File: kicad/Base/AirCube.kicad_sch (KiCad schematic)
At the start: 44 parts, among them P1 USB_C_Plug_USB2.0, Q1 BSS138, U10 ENS210, U2 ENS161, U5 AP2120, U6 AP2205, U7 ESP32-H2-MINI-1

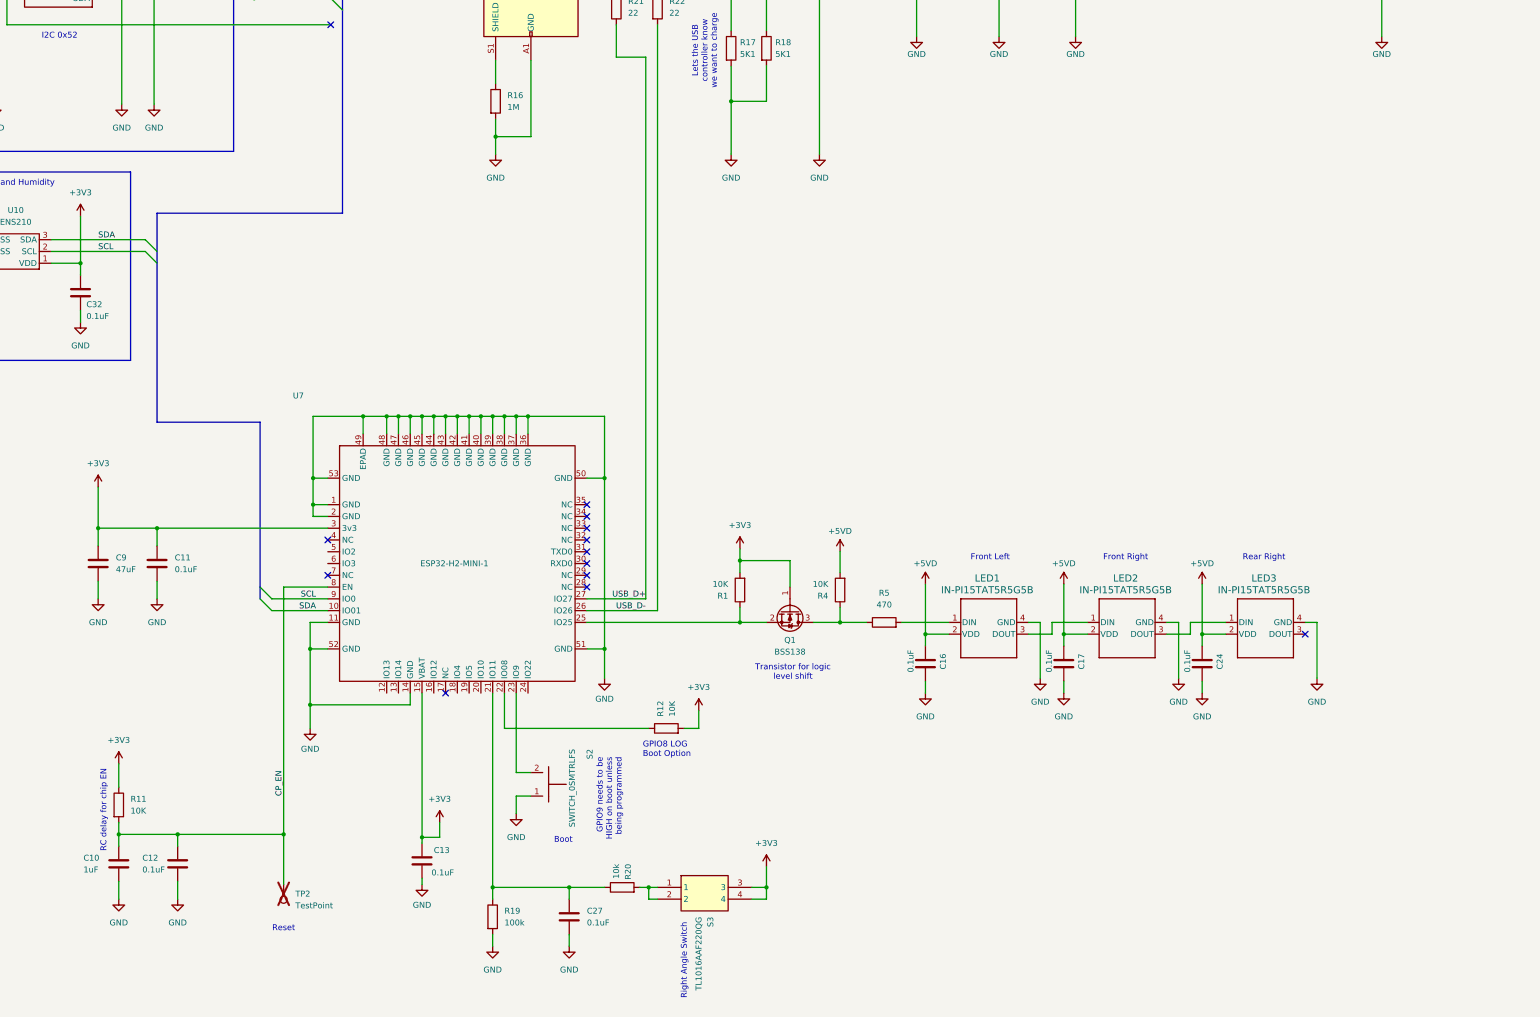
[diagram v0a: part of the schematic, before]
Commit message: Replace H2 schematic with S3 and add PM UART and modem control nets
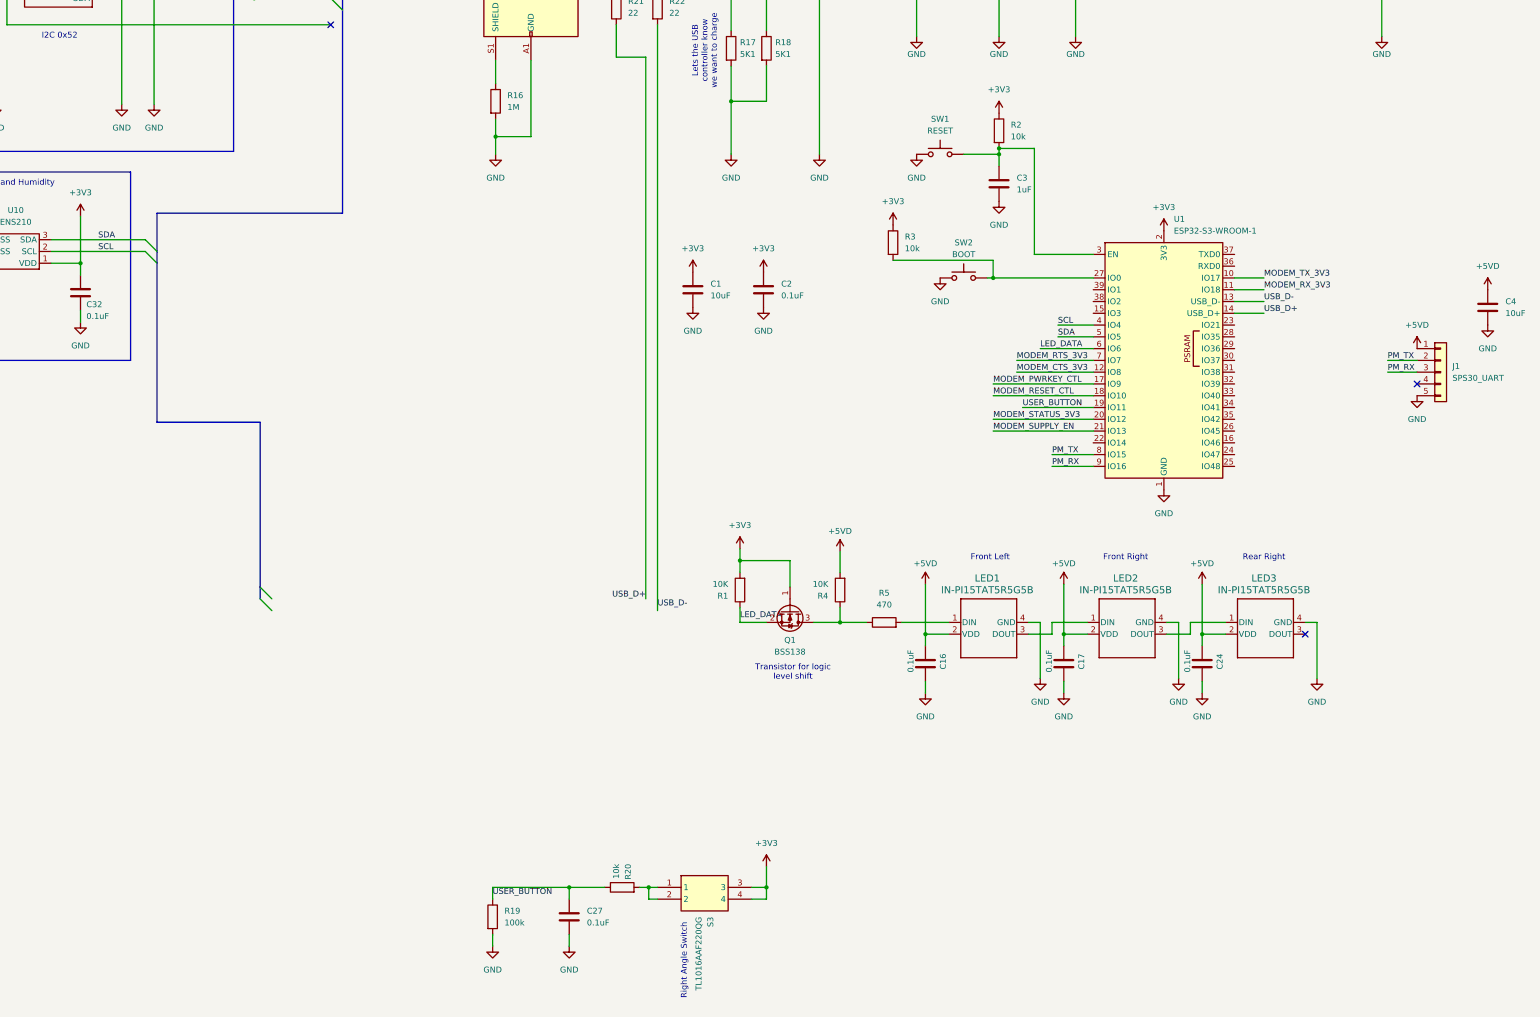
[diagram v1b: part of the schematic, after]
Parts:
- removed C10: 1uF, Capacitor_SMD:C_0603_1608Metric, symbol Device:C
- removed C11, C12, C13: 0.1uF, Capacitor_SMD:C_0603_1608Metric, symbol Device:C
- removed C9: 47uF, Capacitor_SMD:C_0603_1608Metric, symbol Device:C
- removed R11, R12: 10K, Resistor_SMD:R_0603_1608Metric, symbol Device:R
- removed S2: SWITCH_0SMTRLFS, kicad_reformed_custom_IC:SWITCH_0SMTRLFS, symbol custom_IC:TL4100AF240QG_
- removed TP2: TestPoint, TestPoint:TestPoint_Pad_1.5x1.5mm, symbol Connector:TestPoint
- removed U7: ESP32-H2-MINI-1, kicad_reformed_custom_IC:MODULE_ESP32-H2-MINI-1-H2, symbol custom_IC:ESP32-H2-MINI-1
- added C1, C4: 10uF, Capacitor_SMD:C_0805_2012Metric, symbol Device:C
- added C2: 0.1uF, Capacitor_SMD:C_0603_1608Metric, symbol Device:C
- added C3: 1uF, Capacitor_SMD:C_0603_1608Metric, symbol Device:C
- added J1: SPS30_UART, symbol Connector_Generic:Conn_01x05
- added R2, R3: 10k, Resistor_SMD:R_0603_1608Metric, symbol Device:R
- added SW1: RESET, symbol Switch:SW_Push
- added SW2: BOOT, symbol Switch:SW_Push
- added U1: ESP32-S3-WROOM-1, RF_Module:ESP32-S3-WROOM-1, symbol RF_Module:ESP32-S3-WROOM-1
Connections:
- net +3V3: now also C1.1, C2.1, R2.1, R3.1, U1.2 (3V3)
- net +5VD: now also C4.1, J1.1 (Pin_1)
- net GND: now also C1.2, C2.2, C3.2, C4.2, J1.5 (Pin_5), SW1.1, SW2.1, U1.1 (GND), U1.40 (GND), U1.41 (GND)
- net SCL: now also U1.4 (IO4)
- net SDA: now also U1.5 (IO5)
- net USB_D+: now also U1.14 (USB_D+)
- net USB_D-: now also U1.13 (USB_D-)
- net USER_BUTTON: now reaches C27.1, R19.1, R20.1
- net USER_BUTTON: now also U1.19 (IO11)
- net LED_DATA: now reaches Q1.2 (S), R1.1
- net LED_DATA: now also U1.6 (IO6)
- new net: R3.2, SW2.2, U1.27 (IO0)
- new net: C3.1, R2.2, SW1.2, U1.3 (EN)
- new net MODEM_CTS_3V3: U1.12 (IO8)
- new net MODEM_PWRKEY_CTL: U1.17 (IO9)
- new net MODEM_RESET_CTL: U1.18 (IO10)
- new net MODEM_RTS_3V3: U1.7 (IO7)
- new net MODEM_RX_3V3: U1.11 (IO18)
- new net MODEM_STATUS_3V3: U1.20 (IO12)
- new net MODEM_SUPPLY_EN: U1.21 (IO13)
- new net MODEM_TX_3V3: U1.10 (IO17)
- new net PM_RX: J1.3 (Pin_3), U1.9 (IO16)
- new net PM_TX: J1.2 (Pin_2), U1.8 (IO15)
- no-connect marks 14 -> 4
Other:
- note removed: "Boot"
- note removed: "GPIO8 LOG Boot Option"
- note removed: "GPIO9 needs to be HIGH on boot unless being programmed"
- note removed: "RC delay for chip EN"
- note removed: "Reset"

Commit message: Assign connector footprints and ground nano-SIM shell pads
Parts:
- removed P1: USB_C_Plug_USB2.0, kicad_reformed_custom_IC:GCT_USB4105-GF-A, symbol Connector:USB_C_Plug_USB2.0
- removed U5: AP2120, Package_TO_SOT_SMD:SOT-23, symbol custom_IC:AP2120
- removed U6: AP2205, kicad_reformed_custom_IC:AP2204, symbol SAMC21_breakout-rescue:AP2204
- added C10, C30, C36, C6, C7: 33pF, Capacitor_SMD:C_0603_1608Metric, symbol Device:C
- added C11, C13, C25, C29, C35, C8, C9: 100nF, Capacitor_SMD:C_0603_1608Metric, symbol Device:C
- added C12, C20: 10uF, Capacitor_SMD:C_0805_2012Metric, symbol Device:C
- added C18, C26: 22uF, Capacitor_SMD:C_1210_3225Metric, symbol Device:C
- added C19, C28: 3.3nF, Capacitor_SMD:C_0603_1608Metric, symbol Device:C
- added C31, C37: 10pF, Capacitor_SMD:C_0603_1608Metric, symbol Device:C
- added C33, C34: 100uF, Capacitor_Tantalum_SMD:CP_EIA-3528-21_Kemet-B, symbol Device:C_Polarized
- added C38, C39: DNP, Capacitor_SMD:C_0402_1005Metric, symbol Device:C
- added D1, D10, D2, D3, D4, D6, D7, D9: PESD3V3U1UL, Diode_SMD:D_SOD-882, symbol Device:D_Zener
- added D8: TPD1E10B06, Diode_SMD:D_SOD-523, symbol custom_IC:TPD1E10B06DPYR
- added J2: SIM_Card, AirCube_Recovered:nanoSIM_GCT_SIM8060-6-0-14-00_GroundedShell, symbol Connector:SIM_Card
- added J3: LTE_ANT_UFL, Connector_Coaxial:U.FL_Hirose_U.FL-R-SMT-1_Vertical, symbol Connector:Conn_Coaxial
- added J4: MCU_UART_3V3, Connector_PinHeader_2.54mm:PinHeader_1x03_P2.54mm_Vertical, symbol Connector_Generic:Conn_01x03
- added J5: MODEM_USB_SERVICE, Connector_PinHeader_2.54mm:PinHeader_1x04_P2.54mm_Vertical, symbol Connector_Generic:Conn_01x04
- added J6: USB_C_Receptacle_USB2.0_14P, Connector_USB:USB_C_Receptacle_GCT_USB4105-xx-A_16P_TopMnt_Horizontal, symbol Connector:USB_C_Receptacle_USB2.0_14P
- added L1, L2: 2.2uH, Inductor_SMD:L_Coilcraft_XAL4020-XXX, symbol Device:L
- added Q2, Q3: MMBT3904, Package_TO_SOT_SMD:SOT-23, symbol Transistor_BJT:MMBT3904
- added R11, R8: 4.7K, Resistor_SMD:R_0603_1608Metric, symbol Device:R
- added R12: 10k, Resistor_SMD:R_0603_1608Metric, symbol Device:R
- added R13: 120k, Resistor_SMD:R_0603_1608Metric, symbol Device:R
- added R14, R15, R23, R31, R32, R33: 0, Resistor_SMD:R_0603_1608Metric, symbol Device:R
- added R24: 15k, Resistor_SMD:R_0603_1608Metric, symbol Device:R
- added R25, R26: 100k, Resistor_SMD:R_0603_1608Metric, symbol Device:R
- added R27: 374k, Resistor_SMD:R_0603_1608Metric, symbol Device:R
- added R28, R29: 0, Resistor_SMD:R_0805_2012Metric, symbol Device:R
- added R30: 0, Resistor_SMD:R_0402_1005Metric, symbol Device:R
- added R6, R7: 47K, Resistor_SMD:R_0603_1608Metric, symbol Device:R
- added TP1: TP_5V, TestPoint:TestPoint_Pad_D1.5mm, symbol Connector:TestPoint
- added TP2: TP_3V3, TestPoint:TestPoint_Pad_D1.5mm, symbol Connector:TestPoint
- added TP3: TP_MODEM_VBAT, TestPoint:TestPoint_Pad_D1.5mm, symbol Connector:TestPoint
- added TP4: TP_MODEM_1V8, TestPoint:TestPoint_Pad_D1.5mm, symbol Connector:TestPoint
- added TP5: TP_SIM_VDD, TestPoint:TestPoint_Pad_D1.5mm, symbol Connector:TestPoint
- added TP6: TP_GND, TestPoint:TestPoint_Pad_D1.5mm, symbol Connector:TestPoint
- added U3: BG95-M3, RF_GSM:Quectel_BG95, symbol RF_GSM:BG95-M3
- added U4: TXS0108EPW, Package_SO:TSSOP-20_4.4x6.5mm_P0.65mm, symbol Logic_LevelTranslator:TXS0108EPW
- added U5: TLV75518PDBV, Package_TO_SOT_SMD:SOT-23-5, symbol Regulator_Linear:TLV75518PDBV
- added U6: TPS62132, Package_DFN_QFN:VQFN-16-1EP_3x3mm_P0.5mm_EP1.68x1.68mm_ThermalVias, symbol Regulator_Switching:TPS62132
- added U7: TPS62130, Package_DFN_QFN:VQFN-16-1EP_3x3mm_P0.5mm_EP1.68x1.68mm_ThermalVias, symbol Regulator_Switching:TPS62130
- J1: footprint (none) -> Connector_JST:JST_ZH_B5B-ZR_1x05_P1.50mm_Vertical
- LED1, LED2, LED3: footprint custom_IC:IN-PI15_INL -> AirCube_Recovered:IN-PI15_INL
- S3: footprint custom_IC:TL1016AAF220QG -> AirCube_Recovered:TL1016AAF220QG
- SW1, SW2: footprint (none) -> Button_Switch_SMD:SW_SPST_TL3305A
- U10: footprint kicad_reformed_custom_IC:ENS210 -> AirCube_Recovered:ENS210
- U2: footprint kicad_reformed_custom_IC:ENS161 -> AirCube_Recovered:ENS161
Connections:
- net +1V8: now also U5.5 (OUT)
- net +3V3: now also C26.2, C9.1, L2.1, TP2.1, U4.19 (VCCB), U5.1 (IN), U5.3 (EN), U6.14 (VOS), U6.7 (FSW)
- net +5VD: now also C12.1, C13.1, C20.1, C25.1, J6.A4 (VBUS), J6.A9 (VBUS), J6.B4 (VBUS), J6.B9 (VBUS), TP1.1, U6.10 (VIN), U6.11 (VIN), U6.12 (VIN), U6.13 (EN), U7.10 (VIN), U7.11 (VIN), U7.12 (VIN)
- net GND: now also C10.2, C11.2, C12.2, C13.2, C18.1, C19.1, C20.2, C25.2, C26.1, C28.1, C29.2, C30.2, C31.2, C33.2, C34.2, C35.2, C36.2, C37.2, C38.2, C39.2, C6.2, C7.2, C8.2, C9.2, D1.2 (A), D10.2 (A), D2.2 (A), D3.2 (A), D4.2 (A), D6.2 (A), D7.2 (A), D8.2, D9.2 (A), J2.5 (GND), J3.2 (Ext), J4.1 (Pin_1), J5.4 (Pin_4), J6.A1 (GND), J6.A12 (GND), J6.B1 (GND), J6.B12 (GND), Q2.2 (E), Q3.2 (E), R13.2, R25.1, R26.1, R6.2, R7.2, TP6.1, U3.100 (GND), U3.101 (GND), U3.102 (GND), U3.3 (GND), U3.31 (GND), U3.47 (USIM_GND), U3.48 (GND), U3.50 (GND), U3.54 (GND), U3.55 (GND), U3.58 (GND), U3.59 (GND), U3.61 (GND), U3.62 (GND), U3.67 (GND), U3.68 (GND), U3.69 (GND), U3.70 (GND), U3.71 (GND), U3.72 (GND), U3.73 (GND), U3.74 (GND), U3.79 (GND), U3.80 (GND), U3.81 (GND), U3.82 (GND), U3.89 (GND), U3.90 (GND), U3.91 (GND), U4.11 (GND), U5.2 (GND), U6.15 (GND), U6.16 (GND), U6.17 (GND), U6.5 (FB), U6.6 (GND), U6.8 (DEF), U7.15 (GND), U7.16 (GND), U7.17 (GND), U7.6 (GND), U7.8 (DEF)
- net MODEM_CTS_3V3: now also U4.16 (B4)
- net MODEM_PWRKEY_CTL: now also R8.2
- net MODEM_RESET_CTL: now also R11.2
- net MODEM_RTS_3V3: now also U4.17 (B3)
- net MODEM_RX_3V3: now also U4.18 (B2)
- net MODEM_STATUS_3V3: now also U4.15 (B5)
- net MODEM_SUPPLY_EN: now also R25.2, U7.13 (EN)
- net MODEM_TX_3V3: now also U4.20 (B1)
- net at R16.1: now also J6.SH (SHIELD)
- net MCU_DEBUG_RX: now reaches U1.36 (RXD0)
- net MCU_DEBUG_RX: now also J4.3 (Pin_3)
- net MCU_DEBUG_TX: now reaches U1.37 (TXD0)
- net MCU_DEBUG_TX: now also J4.2 (Pin_2)
- net MCU_USB_DM_CONN: now reaches R22.1
- net MCU_USB_DM_CONN: now also D10.1 (K), J6.A7 (D-), J6.B7 (D-)
- net at R17.1: now also J6.B5 (CC2)
- net MCU_USB_DP_CONN: now reaches R21.2
- net MCU_USB_DP_CONN: now also D9.1 (K), J6.A6 (D+), J6.B6 (D+)
- net at R18.1: now also J6.A5 (CC1)
- new net: C28.2, U6.9 (SS/TR)
- new net: R33.1, U3.10 (USB_DM)
- new net: R31.2, U3.8 (VBUS)
- new net: R32.2, U3.9 (USB_DP)
- new net: R12.1, R13.1, U4.10 (OE)
- new net: C19.2, U7.9 (SS/TR)
- new net: Q2.1 (B), R6.1, R8.1
- new net: L2.2, U6.1 (SW), U6.2 (SW), U6.3 (SW)
- new net: Q3.1 (B), R11.1, R7.1
- new net: L1.2, U7.1 (SW), U7.2 (SW), U7.3 (SW)
- new net: R26.2, R27.1, U7.5 (FB)
- new net LTE_RF_ANT: C39.1, J3.1 (In), R30.1
- new net LTE_RF_MODEM: C38.1, R30.2, U3.60 (ANT_MAIN)
- new net MODEM_CTS_1V8: U3.36 (MAIN_CTS), U4.5 (A4)
- new net MODEM_PWRKEY: Q2.3 (C), U3.15 (PWRKEY)
- new net MODEM_RESET_N: Q3.3 (C), U3.17 (~{RESET})
- new net MODEM_RTS_1V8: U3.37 (MAIN_RTS), U4.4 (A3)
- new net MODEM_RXD_1V8: U3.34 (MAIN_RXD), U4.1 (A1)
- new net MODEM_STATUS_1V8: U3.20 (STATUS), U4.6 (A5)
- new net MODEM_TXD_1V8: U3.35 (MAIN_TXD), U4.3 (A2)
- new net MODEM_USB_DM_HOST: D6.1 (K), J5.2 (Pin_2), R33.2
- new net MODEM_USB_DP_HOST: D7.1 (K), J5.3 (Pin_3), R32.1
- new net MODEM_USB_VBUS: D8.1, J5.1 (Pin_1), R31.1
- new net MODEM_VBAT: C18.2, L1.1, R27.2, R28.1, R29.2, TP3.1, U7.14 (VOS), U7.7 (FSW)
- new net MODEM_VBAT_BB: C29.1, C30.1, C31.1, C33.1, R28.2, U3.32 (VBAT_BB), U3.33 (VBAT_BB)
- new net MODEM_VBAT_RF: C34.1, C35.1, C36.1, C37.1, R29.1, U3.52 (VBAT_RF), U3.53 (VBAT_RF)
- new net MODEM_VDD_1V8: C8.1, R12.2, TP4.1, U3.29 (VDD_EXT), U4.2 (VCCA)
- new net SIM_CLK_CARD: C10.1, D2.1 (K), J2.3 (CLK), R15.2
- new net SIM_CLK_MODEM: R15.1, U3.46 (USIM_CLK)
- new net SIM_DATA_CARD: C6.1, D3.1 (K), J2.7 (I/O), R23.2, R24.1
- new net SIM_DATA_MODEM: R23.1, U3.45 (USIM_DATA)
- new net SIM_RST_CARD: C7.1, D1.1 (K), J2.2 (RST), R14.2
- new net SIM_RST_MODEM: R14.1, U3.44 (USIM_RST)
- new net SIM_VDD: C11.1, D4.1 (K), J2.1 (VCC), R24.2, TP5.1, U3.43 (USIM_VDD)
- no-connect marks 4 -> 29
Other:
- moved on the sheet: C1, C2, C27, C4, J1, R16, R19, R20, S3

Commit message: Add cellular and particulate sensor circuitry and project libraries
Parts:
- removed D5: TPD1E10B06, Diode_SMD:D_SOD-523, symbol custom_IC:TPD1E10B06DPYR
- removed R17, R18: 5K1, Resistor_SMD:R_0603_1608Metric, symbol Device:R
- added C40: 100nF, Capacitor_SMD:C_0603_1608Metric, symbol Device:C
- added C41: 1uF, Capacitor_SMD:C_0603_1608Metric, symbol Device:C
- added C42: 10nF, Capacitor_SMD:C_0603_1608Metric, symbol Device:C
- added D11: TPD1E10B06DYAR, Diode_SMD:D_SOD-523, symbol custom_IC:TPD1E10B06DPYR
- added R34: 887k, Resistor_SMD:R_0603_1608Metric, symbol Device:R
- added U11: TUSB320LAIRWBR, Package_DFN_QFN:Texas_X2QFN-12_1.6x1.6mm_P0.4mm, symbol Interface_USB:TUSB320
- added U8: TPS22975DSGR, Package_DFN_QFN:DFN-8-1EP_2x2mm_P0.5mm_EP0.9x1.6mm, symbol AirCube_Custom:TPS22975
- D8: value TPD1E10B06 -> TPD1E10B06DYAR
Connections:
- net +3V3: now also C40.1, U11.12 (VDD)
- net +5VD: now also U8.7 (VOUT), U8.8 (VOUT); no longer J6.A4 (VBUS), J6.A9 (VBUS), J6.B4 (VBUS), J6.B9 (VBUS)
- net GND: now also C40.2, C41.2, C42.2, D11.2, U11.10 (GND), U11.11 (~{EN}), U11.3 (PORT), U11.5 (ADDR), U8.5 (GND), U8.9 (EP)
- net SCL: now also U11.8 (SCL/OUT2)
- net SDA: now also U11.7 (SDA/OUT1)
- net at J6.B5 (CC2): now also U11.2 (CC2)
- net at J6.A5 (CC1): now also U11.1 (CC1)
- new net: C42.1, U8.6 (CT)
- new net: R34.2, U11.4 (VBUS_DET)
- new net USB_VBUS_RAW: C41.1, D11.1, J6.A4 (VBUS), J6.A9 (VBUS), J6.B4 (VBUS), J6.B9 (VBUS), R34.1, U8.1 (VIN), U8.2 (VIN), U8.3 (ON), U8.4 (VBIAS)
- no-connect marks 29 -> 65

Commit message: Route local power stages and join regulator inputs
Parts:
- C14, C15, C16, C17, C21, C22, C23, C24, C27, C32, C5: footprint Capacitor_SMD:C_0603_1608Metric -> AirCube_Recovered:C_0603_1608Metric
- LED1: symbol custom_IC:IN-PI15TAT5R5G5B -> custom_IC:IN-PI15TAT5R5G5B_1
- LED2: symbol custom_IC:IN-PI15TAT5R5G5B -> custom_IC:IN-PI15TAT5R5G5B_2
- Q1: footprint Package_TO_SOT_SMD:SOT-23 -> AirCube_Recovered:SOT-23
- R1, R10, R16, R19, R20, R21, R22, R4, R5, R9: footprint Resistor_SMD:R_0603_1608Metric -> AirCube_Recovered:R_0603_1608Metric
- U1: value ESP32-S3-WROOM-1 -> ESP32-S3-WROOM-1U-N8; footprint RF_Module:ESP32-S3-WROOM-1 -> AirCube_Recovered:ESP32-S3-WROOM-1U_ThermalDrill0.30
- U6, U7: footprint Package_DFN_QFN:VQFN-16-1EP_3x3mm_P0.5mm_EP1.68x1.68mm_ThermalVias -> AirCube_Recovered:TPS6213x_RGT_ThermalDrill0.30
- U8: footprint Package_DFN_QFN:DFN-8-1EP_2x2mm_P0.5mm_EP0.9x1.6mm -> AirCube_Recovered:TPS22975_DSG_TI_LandPattern
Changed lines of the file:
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@@
 			)
 		)
-		(property "Footprint" "Capacitor_SMD:C_0603_1608Metric"
+		(property "Footprint" "AirCube_Recovered:C_0603_1608Metric"
 			(at 296.2402 203.835 0)
 			(hide yes)
@@
 			)
 		)
-		(property "Footprint" "Resistor_SMD:R_0603_1608Metric"
+		(property "Footprint" "AirCube_Recovered:R_0603_1608Metric"
 			(at 104.902 166.37 90)
 			(hide yes)
@@
 			)
 		)
-		(property "Footprint" "Resistor_SMD:R_0603_1608Metric"
+		(property "Footprint" "AirCube_Recovered:R_0603_1608Metric"
 			(at 144.272 83.82 90)
 			(hide yes)
@@
 			)
 		)
-		(property "Value" "ESP32-S3-WROOM-1"
+		(property "Value" "ESP32-S3-WROOM-1U-N8"
 			(at 289.1633 106.68 0)
 			(show_name no)
@@
 			)
 		)
-		(property "Footprint" "RF_Module:ESP32-S3-WROOM-1"
+		(property "Footprint" "AirCube_Recovered:ESP32-S3-WROOM-1U_ThermalDrill0.30"
 			(at 287.02 132.08 0)
 			(hide yes)
@@
 			)
 		)
-		(property "Footprint" "Resistor_SMD:R_0603_1608Metric"
+		(property "Footprint" "AirCube_Recovered:R_0603_1608Metric"
 			(at 218.948 184.15 90)
 			(hide yes)
@@
 			)
 		)
-		(property "Footprint" "Resistor_SMD:R_0603_1608Metric"
+		(property "Footprint" "AirCube_Recovered:R_0603_1608Metric"
 			(at 176.022 58.42 90)
 			(hide yes)
@@
 			)
 		)
-		(property "Footprint" "Capacitor_SMD:C_0603_1608Metric"
+		(property "Footprint" "AirCube_Recovered:C_0603_1608Metric"
 			(at 236.5502 203.835 0)
 			(hide yes)
@@
 			)
 		)
-		(property "Footprint" "Capacitor_SMD:C_0603_1608Metric"
+		(property "Footprint" "AirCube_Recovered:C_0603_1608Metric"
 			(at 266.3952 203.835 0)
 			(hide yes)
@@
 			)
 		)
-		(property "Footprint" "Package_TO_SOT_SMD:SOT-23"
+		(property "Footprint" "AirCube_Recovered:SOT-23"
 			(at 204.47 193.675 0)
 			(hide yes)
@@
 			)
 		)
-		(property "Footprint" "Package_DFN_QFN:VQFN-16-1EP_3x3mm_P0.5mm_EP1.68x1.68mm_ThermalVias"
+		(property "Footprint" "AirCube_Recovered:TPS6213x_RGT_ThermalDrill0.30"
 			(at 254 66.04 0)
 			(hide yes)
@@
 			)
 		)
-		(property "Footprint" "Capacitor_SMD:C_0603_1608Metric"
+		(property "Footprint" "AirCube_Recovered:C_0603_1608Metric"
 			(at 124.1552 170.18 0)
 			(hide yes)
@@
 			)
 		)
-		(property "Footprint" "Package_DFN_QFN:VQFN-16-1EP_3x3mm_P0.5mm_EP1.68x1.68mm_ThermalVias"
+		(property "Footprint" "AirCube_Recovered:TPS6213x_RGT_ThermalDrill0.30"
 			(at 213.36 162.56 0)
 			(hide yes)
@@
 			)
 		)
-		(property "Footprint" "Capacitor_SMD:C_0603_1608Metric"
+		(property "Footprint" "AirCube_Recovered:C_0603_1608Metric"
 			(at 299.4152 42.545 0)
 			(hide yes)
@@
 	)
 	(symbol
-		(lib_name "IN-PI15TAT5R5G5B_1")
-		(lib_id "custom_IC:IN-PI15TAT5R5G5B")
+		(lib_id "custom_IC:IN-PI15TAT5R5G5B_1")
 		(at 248.92 191.77 0)
 		(unit 1)
@@
 			)
 		)
-		(property "Footprint" "Capacitor_SMD:C_0603_1608Metric"
+		(property "Footprint" "AirCube_Recovered:C_0603_1608Metric"
 			(at 268.9352 45.72 0)
 			(hide yes)
@@
 			)
 		)
-		(property "Footprint" "Capacitor_SMD:C_0603_1608Metric"
+		(property "Footprint" "AirCube_Recovered:C_0603_1608Metric"
 			(at 79.7052 46.355 0)
 			(hide yes)
@@
 			)
 		)
-		(property "Footprint" "Capacitor_SMD:C_0603_1608Metric"
+		(property "Footprint" "AirCube_Recovered:C_0603_1608Metric"
 			(at 54.3052 123.825 0)
 			(hide yes)
@@
 			)
 		)
-		(property "Footprint" "Resistor_SMD:R_0603_1608Metric"
+		(property "Footprint" "AirCube_Recovered:R_0603_1608Metric"
 			(at 134.62 161.798 90)
 			(hide yes)
@@
 			)
 		)
-		(property "Footprint" "Capacitor_SMD:C_0603_1608Metric"
+		(property "Footprint" "AirCube_Recovered:C_0603_1608Metric"
 			(at 334.9752 45.72 0)
 			(hide yes)
@@
 			)
 		)
-		(property "Footprint" "Resistor_SMD:R_0603_1608Metric"
+		(property "Footprint" "AirCube_Recovered:R_0603_1608Metric"
 			(at 170.688 58.42 90)
 			(hide yes)
@@
 			)
 		)
-		(property "Footprint" "Capacitor_SMD:C_0603_1608Metric"
+		(property "Footprint" "AirCube_Recovered:C_0603_1608Metric"
 			(at 70.1802 46.355 0)
 			(hide yes)
@@
 			)
 		)
-		(property "Footprint" "Resistor_SMD:R_0603_1608Metric"
+		(property "Footprint" "AirCube_Recovered:R_0603_1608Metric"
 			(at 197.358 184.15 90)
 			(hide yes)
@@
 			)
 		)
-		(property "Footprint" "Resistor_SMD:R_0603_1608Metric"
+		(property "Footprint" "AirCube_Recovered:R_0603_1608Metric"
 			(at 96.647 38.735 90)
 			(hide yes)
@@
 			)
 		)
-		(property "Footprint" "Resistor_SMD:R_0603_1608Metric"
+		(property "Footprint" "AirCube_Recovered:R_0603_1608Metric"
 			(at 226.695 192.913 90)
 			(hide yes)
@@
 			)
 		)
-		(property "Footprint" "Resistor_SMD:R_0603_1608Metric"
+		(property "Footprint" "AirCube_Recovered:R_0603_1608Metric"
 			(at 89.027 38.735 90)
 			(hide yes)
@@
 	)
 	(symbol
-		(lib_name "IN-PI15TAT5R5G5B_2")
-		(lib_id "custom_IC:IN-PI15TAT5R5G5B")
+		(lib_id "custom_IC:IN-PI15TAT5R5G5B_2")
 		(at 278.765 191.77 0)
 		(unit 1)
@@
 			)
 		)
-		(property "Footprint" "Package_DFN_QFN:DFN-8-1EP_2x2mm_P0.5mm_EP0.9x1.6mm"
+		(property "Footprint" "AirCube_Recovered:TPS22975_DSG_TI_LandPattern"
 			(at 93.98 270.51 0)
 			(hide yes)
@@
 			)
 		)
-		(property "Footprint" "Capacitor_SMD:C_0603_1608Metric"
+		(property "Footprint" "AirCube_Recovered:C_0603_1608Metric"
 			(at 234.6452 45.72 0)
 			(hide yes)
